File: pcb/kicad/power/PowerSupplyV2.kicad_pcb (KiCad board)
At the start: 2 copper layers, 35 parts, among them J1 12VWallWartVin, J2 OpAmpVsupply, J3 BackUpPower, J5 ResistorPinTest, J6 VSupplyLCDDisplay, J7 Vout1, J8 Vout2, J9 Vout3, U2 LM317H, U3 LM2574

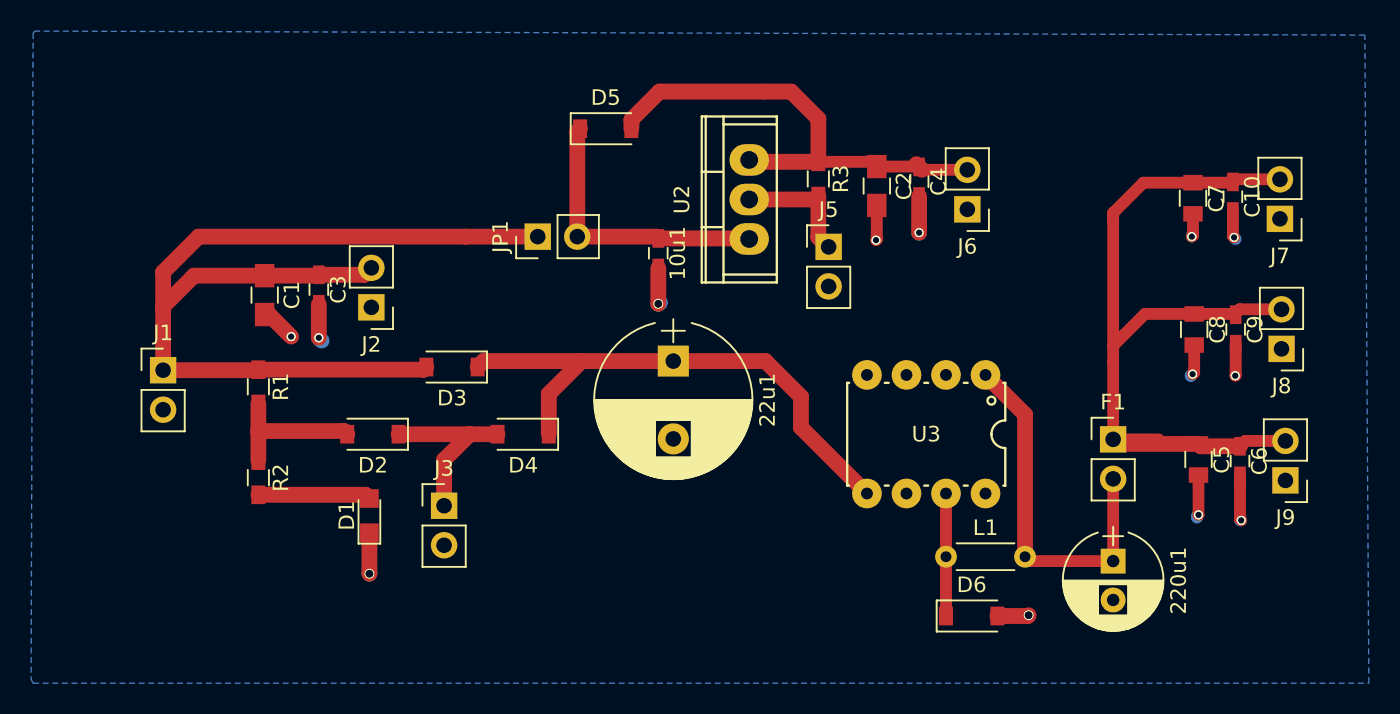
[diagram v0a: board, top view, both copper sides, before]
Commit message: Add power supply to tile
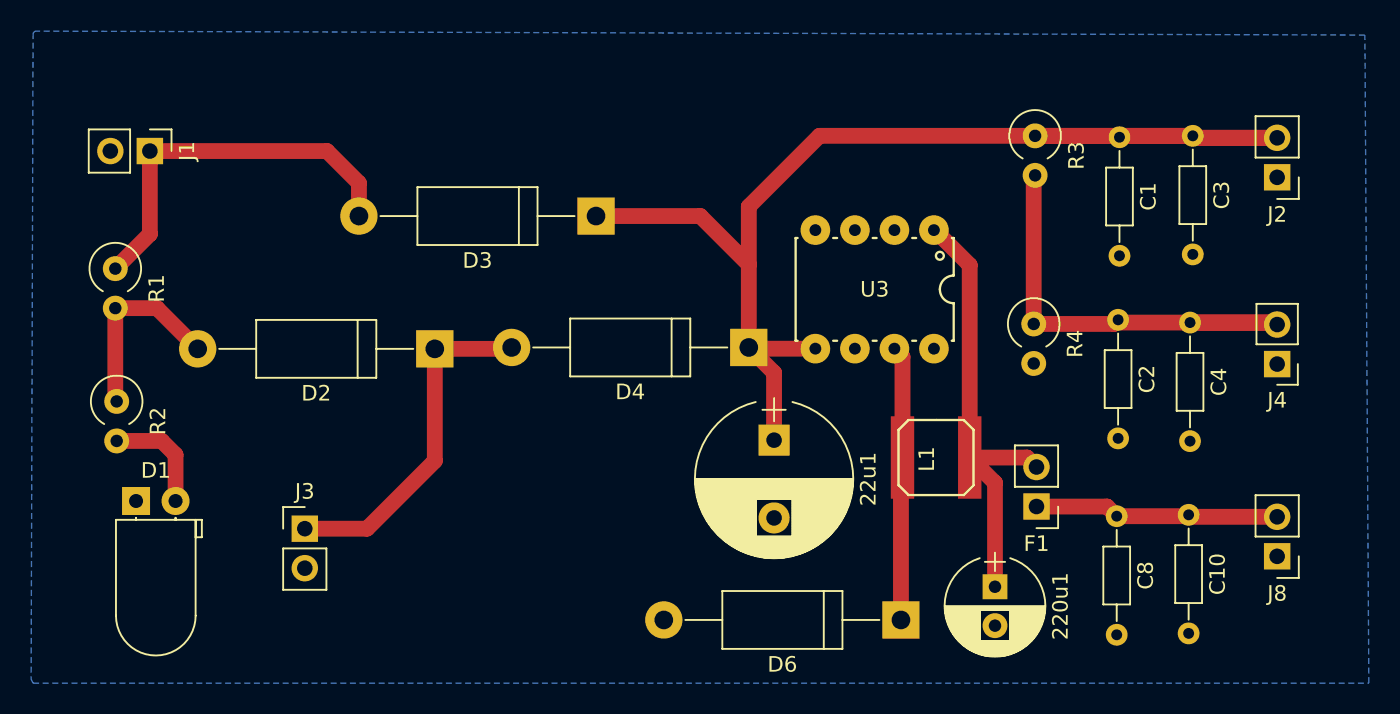
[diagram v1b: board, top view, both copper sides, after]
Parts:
- removed 10u1: C, Capacitors_SMD:C_0603_HandSoldering
- removed C5, C7: 1u, Capacitors_SMD:C_0805
- removed C6, C9: 0.1u, Capacitors_SMD:C_0603_HandSoldering
- removed D5: 11DQ05, Diodes_SMD:D_SOD-123
- removed J5: ResistorPinTest, Pin_Headers:Pin_Header_Straight_1x02_Pitch2.54mm
- removed J6: VSupplyLCDDisplay, Pin_Headers:Pin_Header_Straight_1x02_Pitch2.54mm
- removed J7: Vout1, Pin_Headers:Pin_Header_Straight_1x02_Pitch2.54mm
- removed J9: Vout3, Pin_Headers:Pin_Header_Straight_1x02_Pitch2.54mm
- removed JP1: Jumper, Pin_Headers:Pin_Header_Straight_1x02_Pitch2.54mm
- removed U2: LM317H, Power_Integrations:TO-220
- added J4: Display, Pin_Headers:Pin_Header_Straight_1x02_Pitch2.54mm, F.Cu at (180.3, 92.0)
- added R4: 120, Resistors_THT:R_Axial_DIN0309_L9.0mm_D3.2mm_P2.54mm_Vertical, F.Cu at (164.6, 89.4)
- C1, C2: footprint Capacitors_SMD:C_0805_HandSoldering -> Resistors_THT:R_Axial_DIN0204_L3.6mm_D1.6mm_P7.62mm_Horizontal
- C10, C3, C4: footprint Capacitors_SMD:C_0603_HandSoldering -> Resistors_THT:R_Axial_DIN0204_L3.6mm_D1.6mm_P7.62mm_Horizontal
- C8: footprint Capacitors_SMD:C_0805 -> Resistors_THT:R_Axial_DIN0204_L3.6mm_D1.6mm_P7.62mm_Horizontal
- D1: footprint LEDs:LED_0805 -> LEDs:LED_D5.0mm_Horizontal_O1.27mm_Z3.0mm
- D2, D3, D4, D6: footprint Diodes_SMD:D_SOD-123 -> Diodes_THT:D_DO-15_P15.24mm_Horizontal
- J8: value Vout2 -> Ucontroller
- L1: footprint Resistors_THT:R_Axial_DIN0204_L3.6mm_D1.6mm_P5.08mm_Horizontal -> Inductors:SELF-WE-TPC_M
- R1, R2: footprint Resistors_SMD:R_0603_HandSoldering -> Resistors_THT:R_Axial_DIN0309_L9.0mm_D3.2mm_P2.54mm_Vertical
- R3: value 220 -> 160; footprint Resistors_SMD:R_0603_HandSoldering -> Resistors_THT:R_Axial_DIN0309_L9.0mm_D3.2mm_P2.54mm_Vertical
- moved J2 58.8 mm to (180.3, 80.0)
- moved C3 57.0 mm to (174.9, 77.3)
- moved C1 55.9 mm to (170.2, 77.4)
- moved C10 20.6 mm to (174.6, 101.7)
- moved C4 19.6 mm to (174.7, 89.3)
- moved C2 17.7 mm to (170.1, 89.2)
- moved D4 15.5 mm to (146.3, 90.9)
- moved D1 15.0 mm to (106.9, 100.8), turned to 0 degrees
- moved R3 14.2 mm to (164.7, 77.3)
- moved J1 14.1 mm to (107.8, 78.3), turned to 270 degrees
- moved D3 13.4 mm to (136.5, 82.5)
- moved J8 13.3 mm to (180.3, 104.4)
- moved C8 13.0 mm to (170.0, 101.8)
- moved R1 11.9 mm to (105.6, 85.9)
- moved R2 10.3 mm to (105.7, 94.4)
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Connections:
- C1 pad 1: Net-(C1-Pad1) -> Net-(22u1-Pad1)
- C3 pad 1: Net-(C1-Pad1) -> Net-(22u1-Pad1)
- D3 pad 2: Net-(C1-Pad1) -> Net-(D3-Pad2)
- J1 pad 1: Net-(C1-Pad1) -> Net-(D3-Pad2)
- J2 pad 2: Net-(C1-Pad1) -> Net-(22u1-Pad1)
- R1 pad 1: Net-(C1-Pad1) -> Net-(D3-Pad2)
- R3 pad 1: Net-(C2-Pad1) -> Net-(22u1-Pad1)
- R3 pad 2: Net-(J5-Pad1) -> Net-(C2-Pad1)
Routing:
- net Net-(C1-Pad1): track 62.8 -> 0.00 mm
- net Net-(22u1-Pad1): track 35.4 -> 82.6 mm
- net Net-(C10-Pad1): track 52.5 -> 15.7 mm
- net GND: track 29.8 -> 0.00 mm, vias 13 -> 0
- net Net-(D3-Pad2): track 0.00 -> 24.9 mm
- net Net-(10u1-Pad1): track 18.1 -> 0.00 mm
- net Net-(D2-Pad1): track 11.6 -> 22.3 mm
- net Net-(D6-Pad1): track 7.87 -> 17.7 mm
- net Net-(J5-Pad1): track 8.02 -> 0.00 mm
- net Net-(220u1-Pad1): track 23.8 -> 29.1 mm
- net Net-(D2-Pad2): track 9.44 -> 12.4 mm
- net Net-(C2-Pad1): track 31.6 -> 31.0 mm

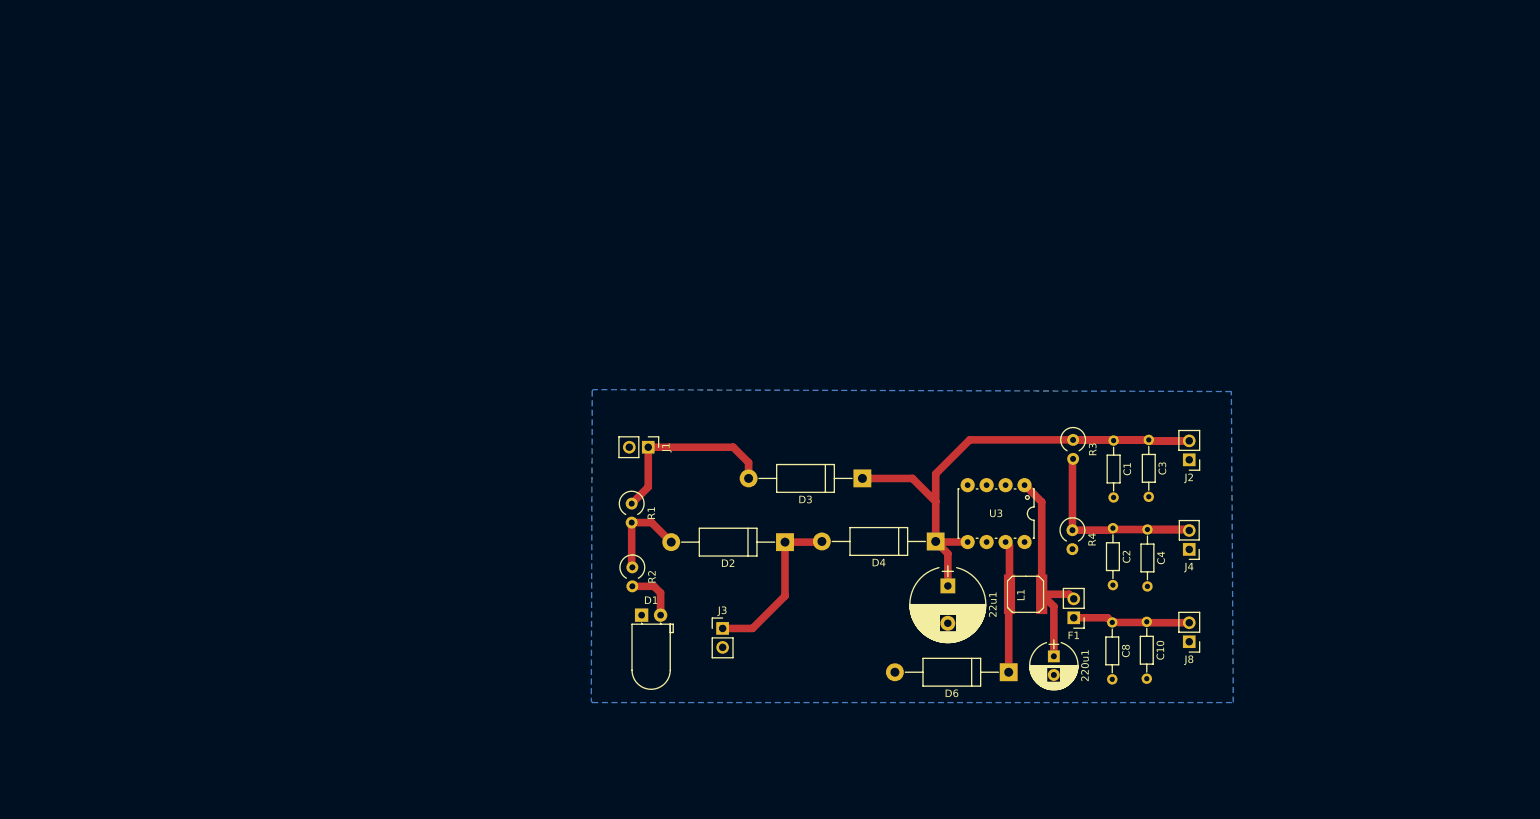
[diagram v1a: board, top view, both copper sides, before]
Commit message: Tile uC and antenna boards
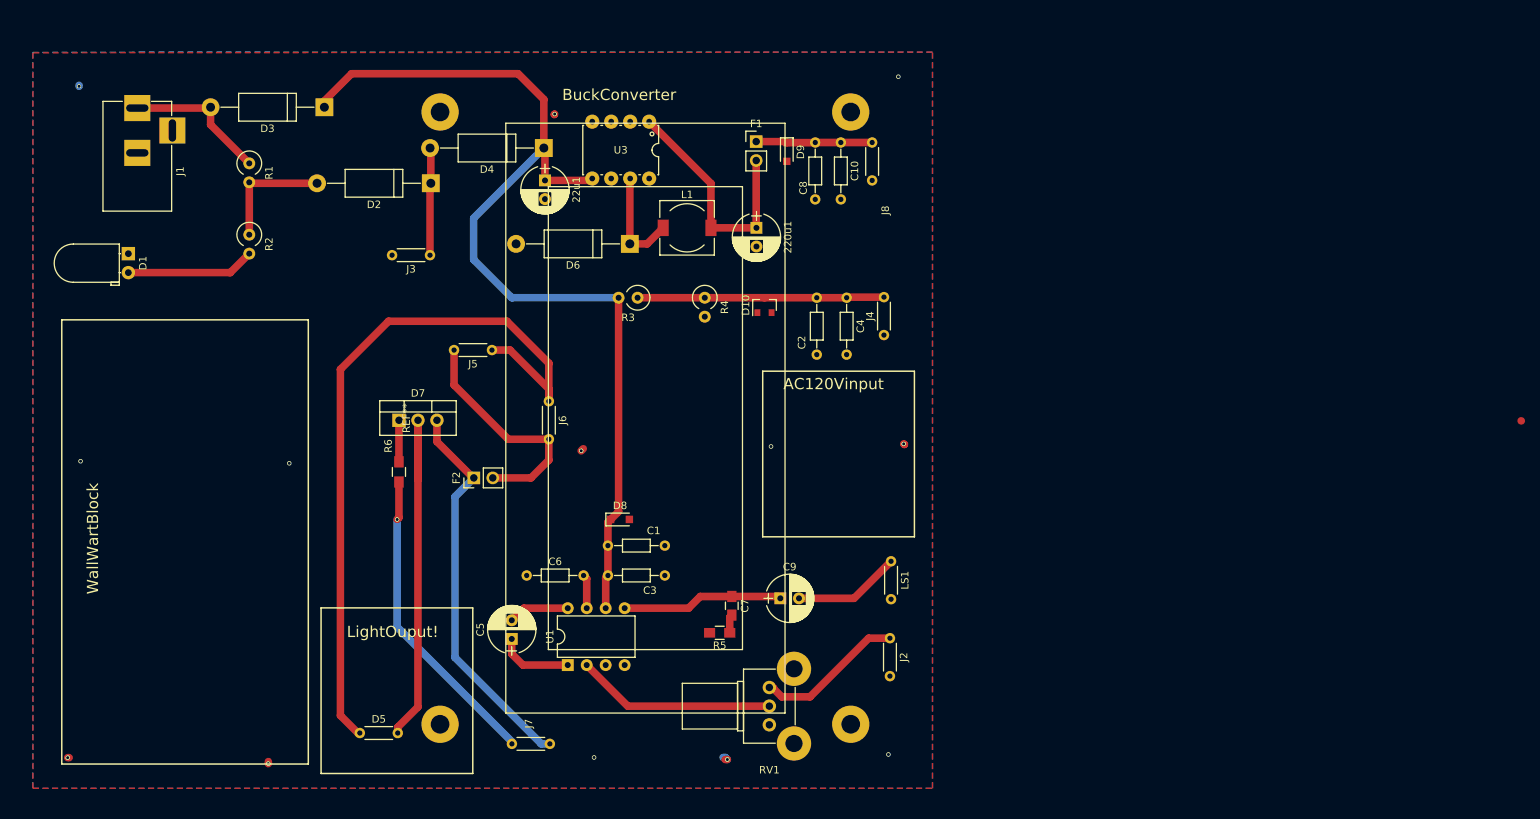
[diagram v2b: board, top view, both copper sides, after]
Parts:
- added C5: 10u, Capacitors_THT:CP_Radial_D6.3mm_P2.50mm, F.Cu at (89.5, 104.0)
- added C6: 0.1u, Resistors_THT:R_Axial_DIN0204_L3.6mm_D1.6mm_P7.62mm_Horizontal, F.Cu at (91.5, 95.5)
- added C7: 0.05u, Capacitors_SMD:C_0805_HandSoldering, F.Cu at (119.0, 99.6)
- added C9: 250u, Capacitors_THT:CP_Radial_D6.3mm_P2.50mm, F.Cu at (125.5, 98.6)
- added D10: 5Vz, Diodes_SMD:D_SOT-23_ANK, F.Cu at (123.4, 59.3)
- added D5: 6.6WLED, Resistors_THT:R_Axial_DIN0204_L3.6mm_D1.6mm_P5.08mm_Horizontal, F.Cu at (69.2, 116.6)
- added D7: 15AmpTriac, TO_SOT_Packages_THT:TO-220_Vertical, F.Cu at (74.5, 74.7)
- added D8: 12Vz, Diodes_SMD:D_SOD-323_HandSoldering, F.Cu at (104.0, 88.0)
- added D9: 3.3Vz, Diodes_SMD:D_SOD-323_HandSoldering, F.Cu at (126.4, 38.8)
- added F2: 3Amps, Pin_Headers:Pin_Header_Straight_1x02_Pitch2.54mm, F.Cu at (84.5, 82.4)
- added J5: WallWartACin, Resistors_THT:R_Axial_DIN0204_L3.6mm_D1.6mm_P5.08mm_Horizontal, F.Cu at (86.9, 65.3)
- added J6: 120VAC, Resistors_THT:R_Axial_DIN0204_L3.6mm_D1.6mm_P5.08mm_Horizontal, F.Cu at (94.5, 72.2)
- added J7: Uc3.3VSignal, Resistors_THT:R_Axial_DIN0204_L3.6mm_D1.6mm_P5.08mm_Horizontal, F.Cu at (94.7, 118.0)
- added LS1: Speaker, Resistors_THT:R_Axial_DIN0204_L3.6mm_D1.6mm_P5.08mm_Horizontal, F.Cu at (140.3, 93.6)
- added R5: 10, Resistors_SMD:R_0805_HandSoldering, F.Cu at (117.4, 103.2)
- added R6: 120, Resistors_SMD:R_0805_HandSoldering, F.Cu at (74.4, 81.6)
- added REF**: CFAH1604A, New Folder With Items:CFAH1604A, F.Cu at (107.5, 74.4)
- added RV1: 10k, Potentiometers:Potentiometer_Alps_RK09K_Vertical, F.Cu at (124.0, 110.5)
- added U1: LM386, Housings_DIP:DIP-8_W7.62mm, F.Cu at (97.0, 107.5)
- 22u1: footprint Capacitors_THT:CP_Radial_D10.0mm_P5.00mm -> Capacitors_THT:CP_Radial_D6.3mm_P2.50mm
- J1: footprint Pin_Headers:Pin_Header_Straight_1x02_Pitch2.54mm -> Connectors:BARREL_JACK
- J2: value OpAmpVsupply -> AudioInput; footprint Pin_Headers:Pin_Header_Straight_1x02_Pitch2.54mm -> Resistors_THT:R_Axial_DIN0204_L3.6mm_D1.6mm_P5.08mm_Horizontal
- J3: value BackUpPower -> BackUpPower12V; footprint Pin_Headers:Pin_Header_Straight_1x02_Pitch2.54mm -> Resistors_THT:R_Axial_DIN0204_L3.6mm_D1.6mm_P5.08mm_Horizontal
- J4: value Display -> Display5V; footprint Pin_Headers:Pin_Header_Straight_1x02_Pitch2.54mm -> Resistors_THT:R_Axial_DIN0204_L3.6mm_D1.6mm_P5.08mm_Horizontal
- J8: value Ucontroller -> Ucontroller3.3; footprint Pin_Headers:Pin_Header_Straight_1x02_Pitch2.54mm -> Resistors_THT:R_Axial_DIN0204_L3.6mm_D1.6mm_P5.08mm_Horizontal
- L1: footprint Inductors:SELF-WE-TPC_M -> Choke_SMD:Choke_SMD_7.3x7.3_H3.5
- moved D3 87.5 mm to (64.5, 32.8)
- moved D1 84.1 mm to (38.2, 52.4), turned to 270 degrees
- moved J1 82.1 mm to (39.4, 32.9), turned to 90 degrees
- moved F1 76.7 mm to (122.3, 37.4), turned to 0 degrees
- moved D6 76.6 mm to (105.4, 51.1)
- moved 22u1 76.6 mm to (94.0, 42.6)
- moved C10 76.2 mm to (133.6, 37.5)
- moved C8 75.6 mm to (130.2, 37.5)
- moved J8 75.0 mm to (137.8, 42.6), turned to 90 degrees
- moved D4 74.4 mm to (93.8, 38.2)
- moved U3 70.0 mm to (104.1, 38.5)
- moved 220u1 69.9 mm to (122.3, 48.9)
- moved R1 68.6 mm to (54.4, 40.3)
- moved R2 68.0 mm to (54.4, 49.9)
- moved D2 67.5 mm to (78.7, 43.0)
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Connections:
- C1 pad 1: Net-(22u1-Pad1) -> GND
- C1 pad 2: GND -> Net-(22u1-Pad1)
- C3 pad 1: Net-(22u1-Pad1) -> GND
- C3 pad 2: GND -> Net-(22u1-Pad1)
- J2 pad 1: GND -> Net-(J2-Pad1)
- J2 pad 2: Net-(22u1-Pad1) -> GND
- R3 pad 1: Net-(22u1-Pad1) -> Net-(C2-Pad1)
- R3 pad 2: Net-(C2-Pad1) -> Net-(22u1-Pad1)
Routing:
- net Net-(D5-Pad1): track 0.00 -> 99.4 mm
- net Net-(D7-Pad3): track 0.00 -> 52.7 mm
- net Net-(D5-Pad2): track 0.00 -> 51.0 mm
- net Net-(22u1-Pad1): track 82.6 -> 133.2 mm
- net Net-(J7-Pad2): track 0.00 -> 41.5 mm, vias 0 -> 1
- net Net-(F2-Pad2): track 0.00 -> 31.7 mm
- net Net-(RV1-Pad2): track 0.00 -> 26.7 mm
- net Net-(C7-Pad1): track 0.00 -> 21.9 mm
- net Net-(J2-Pad1): track 0.00 -> 21.1 mm
- net Net-(C9-Pad2): track 0.00 -> 14.4 mm
- net Net-(D1-Pad2): track 7.12 -> 17.2 mm
- net Net-(C5-Pad1): track 0.00 -> 10.1 mm
- net Net-(C5-Pad2): track 0.00 -> 8.17 mm
- net Net-(D2-Pad1): track 22.3 -> 14.6 mm
- net Net-(D7-Pad1): track 0.00 -> 5.57 mm
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- added copper zone on F.Cu, net GND
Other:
- board text added: "AC120Vinput"
- board text added: "BuckConverter"
- board text added: "LightOuput!"
- board text added: "WallWartBlock"
